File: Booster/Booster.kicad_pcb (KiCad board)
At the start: 2 copper layers, 100 x 100 mm, 113 parts, among them IC401 SN754410, J101 Track, J301 15VDC, J601 StatusLED, J701 Conn_01x04, P201 CONN_01X02, P202 CONN_01X02, P601 ~OVERCURRENT_OUT, P602 ~OVERCURRENT_OUT_OP, P603 MSTR_SW, P604 MSTR_SW_OUT, P605 MSTR_SW_OUT_OP, P606 ~DRIVER_ENABLE_OUT_OP, P607 ~DRIVER_ENABLE_OUT, P701 REVERSER_OUT, P702 REVERSER_OUT_OP, Q601 BC807-40, Q602 BC807-40, Q603 BC807-40, Q604 BC817-40, Q701 BC817-40, SW601 DIP, U201 6N137, U203 LM339, U301 LM7805_TO220, U501 LM338, U502 LM358, U503 NE555, U504 74HC08, U602 PC817, U603 PC817, U604 PC817, U701 74HC86, U702 PC817

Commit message: Still working on PCB layout
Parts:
- added REF**: 1pin, Connectors:1pin, F.Cu at (130.0, 145.0)
- added REF**: 1pin, Connectors:1pin, F.Cu at (45.0, 145.0)
- moved R708 222.6 mm to (44.0, 117.0)
- moved D701 207.8 mm to (44.0, 108.0)
- moved P202 188.3 mm to (109.0, 85.5), turned to 90 degrees
- moved R614 170.6 mm to (41.0, 90.0)
- moved D601 165.3 mm to (47.5, 98.0), turned to 180 degrees
- moved R603 160.5 mm to (48.0, 113.0)
- moved R607 158.3 mm to (49.0, 90.0)
- moved U702 156.1 mm to (97.0, 92.6), turned to 90 degrees
- moved R608 155.0 mm to (48.0, 79.0)
- moved Q701 150.3 mm to (94.0, 89.0)
- moved P701 149.7 mm to (95.0, 76.5), turned to 90 degrees
- moved U602 147.1 mm to (55.5, 100.6), turned to 90 degrees
- moved R705 145.0 mm to (123.0, 83.0)
- moved R601 143.2 mm to (54.0, 110.0)
- moved J601 143.1 mm to (49.0, 85.0), turned to 180 degrees
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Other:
- outline, holes or cut-outs redrawn

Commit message: Starting to add traces. Minor schematic changes to aid routing.
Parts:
- added REF**: Heatshield, Trainiot:Single_Pin_Heatshield, F.Cu at (50.5, 119.5)
- added TP511: TEST, Measurement_Points:Measurement_Point_Round-TH_Small, B.Cu at (123.5, 138.0)
- C301, C302, C502, C506, D301, IC401, J101, J301, RV501, RV502, RV503, RV504, RV701, TP501, TP503, TP504, TP505, TP507, U501: moved to B.Cu
- R508, R509: footprint Resistors_SMD:R_0805 -> Resistors_THT:R_Axial_DIN0207_L6.3mm_D2.5mm_P7.62mm_Horizontal
- U201: footprint Housings_DIP:DIP-8_W7.62mm -> Housings_DIP:SMDIP-8_W9.53mm_Clearance8mm
- U301: footprint TO_SOT_Packages_THT:TO-220-3_Vertical -> TO_SOT_Packages_SMD:SOT-89-3
- U602, U603, U604, U702: footprint Housings_DIP:DIP-4_W7.62mm -> Housings_DIP:SMDIP-4_W9.53mm_Clearance8mm
- moved D201 220.7 mm to (82.8, 121.5)
- moved R204 215.6 mm to (93.5, 140.4), turned to 90 degrees
- moved D202 214.6 mm to (94.5, 97.0)
- moved R205 211.0 mm to (90.0, 135.4), turned to 90 degrees
- moved C202 206.9 mm to (101.0, 107.0)
- moved C201 200.2 mm to (114.0, 97.5)
- moved C401 189.2 mm to (43.5, 140.0)
- moved R704 181.9 mm to (83.0, 107.5)
- moved C402 172.2 mm to (65.0, 131.5)
- moved R707 163.1 mm to (94.5, 83.5)
- moved R702 154.1 mm to (114.0, 87.5)
- moved R609 110.4 mm to (82.0, 94.5)
- moved R610 82.0 mm to (119.0, 83.0)
- moved C601 58.1 mm to (167.8, 63.3)
- moved R201 58.1 mm to (264.5, 80.3)
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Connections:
- R502 pad 1: Net-(R502-Pad1) -> GND
- R502 pad 2: Net-(R501-Pad1) -> Net-(R502-Pad2)
- REF** pad 1: (no net) -> GND (x2)
- RV501 pad 1: GND -> Net-(R502-Pad2)
- RV501 pad 2: GND -> Net-(R502-Pad2)
- RV501 pad 3: Net-(R502-Pad1) -> Net-(R501-Pad1)
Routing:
- net +5V: track 0.00 -> 96.7 mm
- net +15V: track 0.00 -> 57.3 mm
- net /Driver/VCC_DRIVER: track 0.00 -> 41.0 mm
- net Net-(R503-Pad2): track 0.00 -> 38.5 mm, vias 0 -> 2
- net Net-(R505-Pad1): track 0.00 -> 31.7 mm
- net Net-(C507-Pad1): track 0.00 -> 30.4 mm
- net /Driver/DRIVER_ENABLE: track 0.00 -> 28.9 mm
- net GND: track 0.00 -> 23.4 mm
- net Net-(R503-Pad1): track 0.00 -> 20.4 mm
- net /Driver/TrackB: track 0.00 -> 16.9 mm
- net /Driver/TrackA: track 0.00 -> 15.8 mm
- net Net-(C502-Pad1): track 0.00 -> 14.4 mm
- net /Driver/DRIVER_SIGNAL: track 0.00 -> 14.2 mm
- net /DCC Input/REF_1.35V: track 0.00 -> 7.71 mm
- net Net-(R505-Pad2): track 0.00 -> 7.66 mm
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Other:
- net class HighAmp added: clearance 0.5, trace_width 3.5, via_dia 0.8, via_drill 0.6
- board text added: "15VDC"
- board text added: "A-Track-B"
- board text added: "GND"

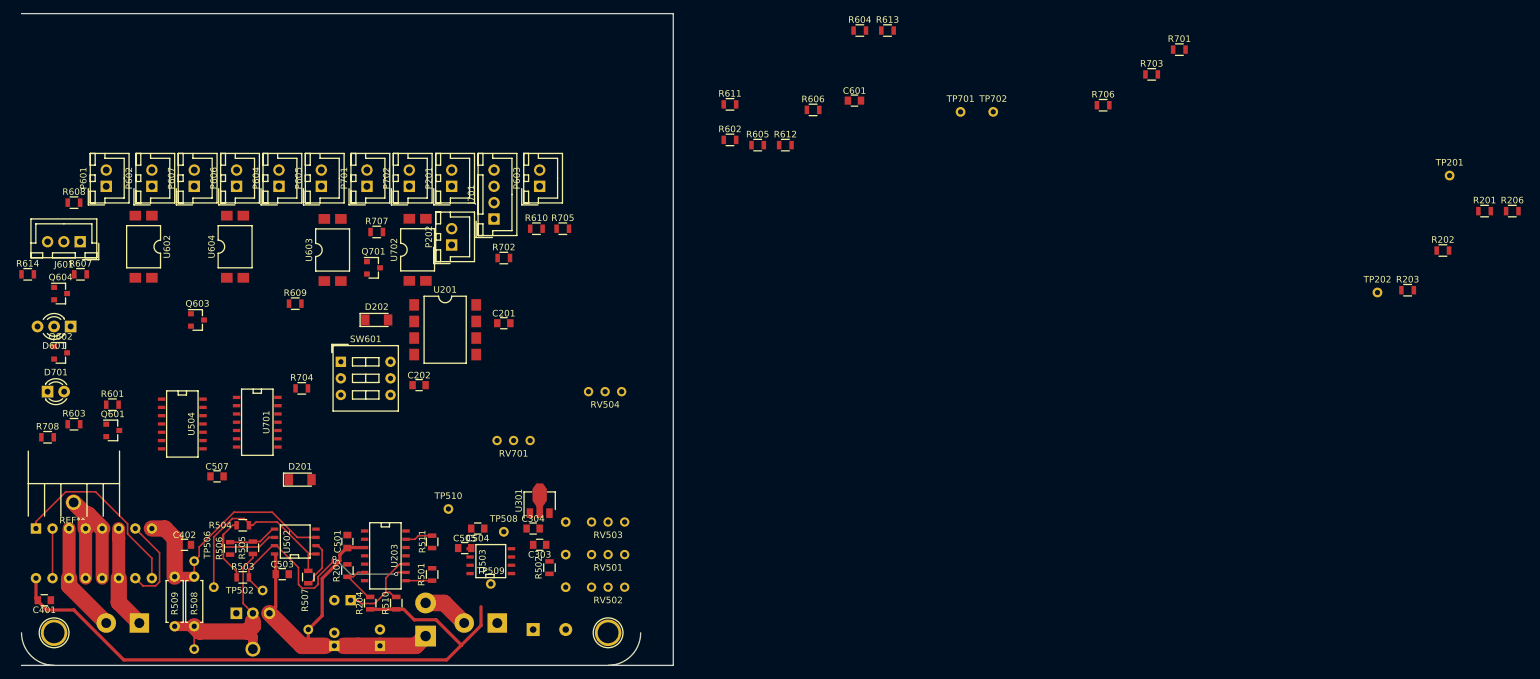
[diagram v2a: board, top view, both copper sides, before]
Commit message: First full layout pass of the PCB.
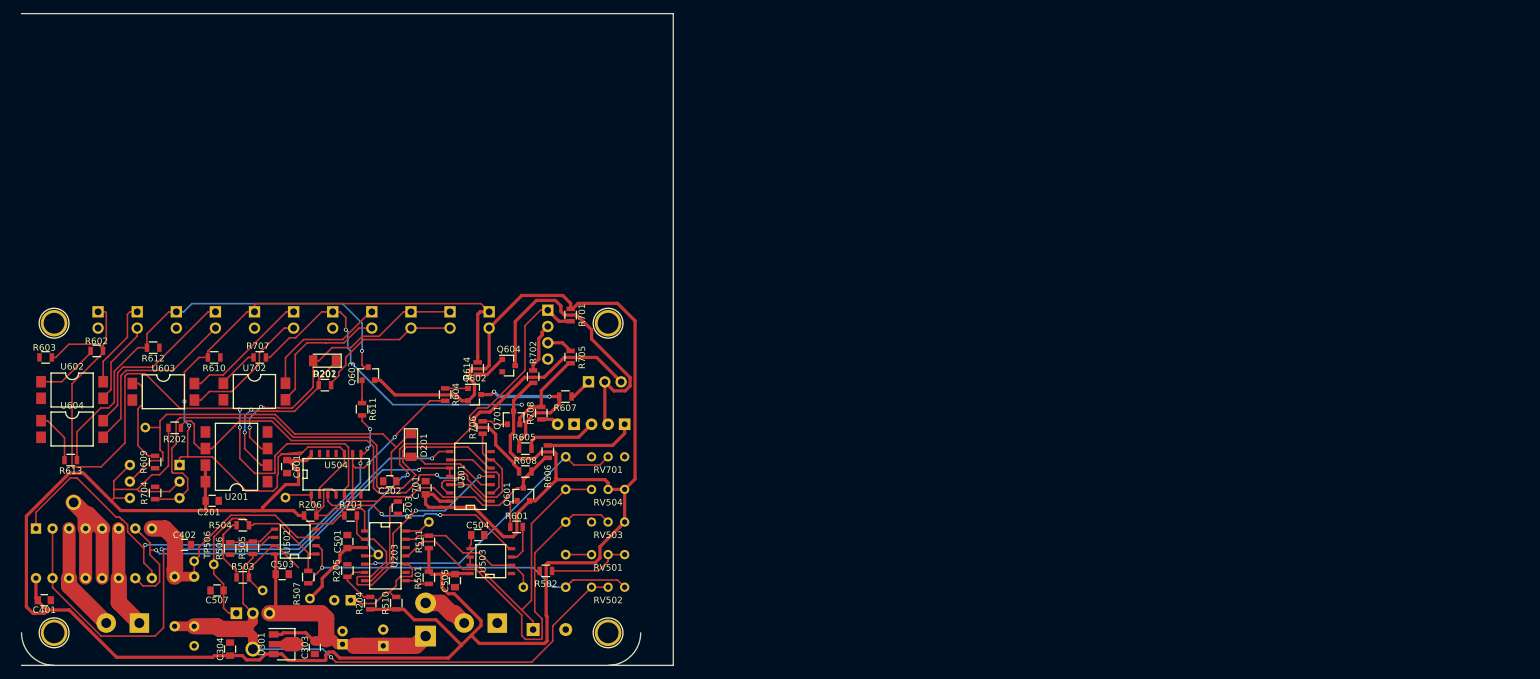
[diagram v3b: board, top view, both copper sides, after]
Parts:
- added C701: 100nF, Capacitors_SMD:C_0805, F.Cu at (102.0, 122.8)
- added REF**: 1pin, Connectors:1pin, F.Cu at (45.0, 97.5)
- added REF**: 1pin, Connectors:1pin, F.Cu at (130.0, 97.5)
- D601, D701, J601, J701, P201, P202, P601, P602, P603, P604, P605, P606, P607, P701, P702, R508, R509, REF**, SW601, TP201, TP202, TP502, TP508, TP509, TP510, TP701, TP702: moved to B.Cu
- moved TP201 203.8 mm to (59.0, 113.5)
- moved R202 196.5 mm to (63.5, 113.5)
- moved R206 190.3 mm to (84.3, 127.0)
- moved R201 179.9 mm to (86.5, 107.0)
- moved TP202 170.5 mm to (80.5, 124.2)
- moved R203 158.5 mm to (97.8, 125.8), turned to 270 degrees
- moved R613 141.6 mm to (47.5, 118.5), turned to 180 degrees
- moved R703 140.3 mm to (90.5, 127.0)
- moved TP702 116.2 mm to (94.8, 133.0)
- moved R706 107.3 mm to (110.8, 113.5), turned to 270 degrees
- moved C601 103.6 mm to (80.8, 119.5), turned to 270 degrees
- moved R602 102.4 mm to (51.5, 101.8)
- moved R701 101.9 mm to (124.2, 96.2), turned to 90 degrees
- moved R612 101.9 mm to (60.2, 101.2), turned to 180 degrees
- moved D601 86.3 mm to (132.5, 113.0)
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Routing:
- net +5V: track 96.7 -> 457.1 mm
- net /Status/STATUS_GREEN_LED: track 0.00 -> 150.1 mm, vias 0 -> 2
- net /Overcurrent Detector/MSTR_SW: track 0.00 -> 120.9 mm, vias 0 -> 2
- net Net-(IC401-Pad15): track 7.62 -> 92.3 mm, vias 0 -> 2
- net Net-(R704-Pad1): track 0.00 -> 83.9 mm
- net Net-(C202-Pad1): track 0.00 -> 77.6 mm
- net Net-(P607-Pad1): track 0.00 -> 69.0 mm, vias 0 -> 1
- net /DCC Input/DCC: track 0.00 -> 68.1 mm, vias 0 -> 2
- net Net-(P701-Pad1): track 0.00 -> 65.3 mm, vias 0 -> 2
- net /Reversing/PhotoDiode: track 0.00 -> 63.2 mm, vias 0 -> 1
- net Net-(RV503-Pad2): track 0.00 -> 57.6 mm
- net Net-(R505-Pad1): track 31.7 -> 89.3 mm, vias 0 -> 1
- net /Driver/DRIVER_SIGNAL: track 14.2 -> 67.2 mm, vias 0 -> 2
- net /Driver/DRIVER_ENABLE: track 28.9 -> 80.9 mm, vias 0 -> 4
- net Net-(R507-Pad1): track 7.40 -> 56.0 mm, vias 0 -> 1
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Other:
- rule trace_min: 0.254 -> 0.25

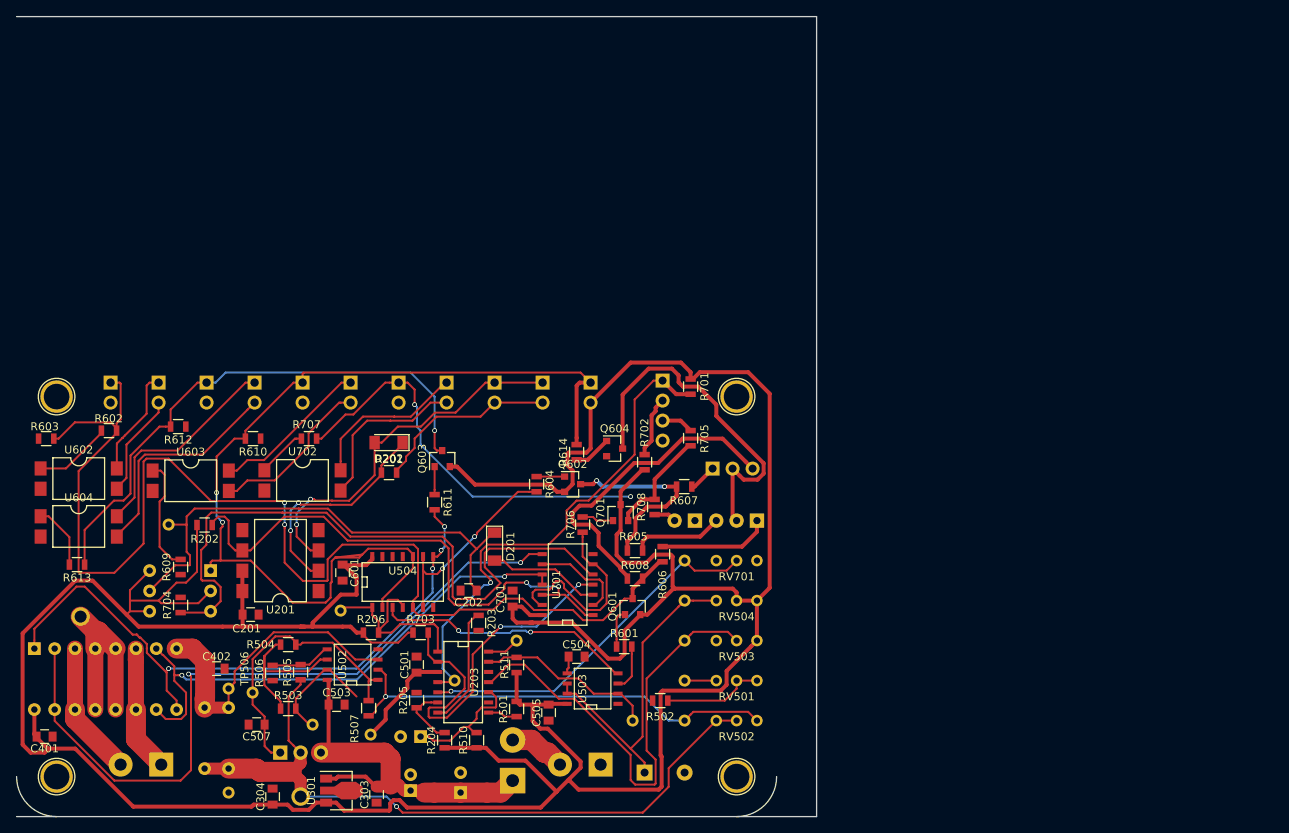
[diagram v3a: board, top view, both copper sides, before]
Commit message: Made board slightly larger to have more space along the edge. It is now 9.7 x 6 cm
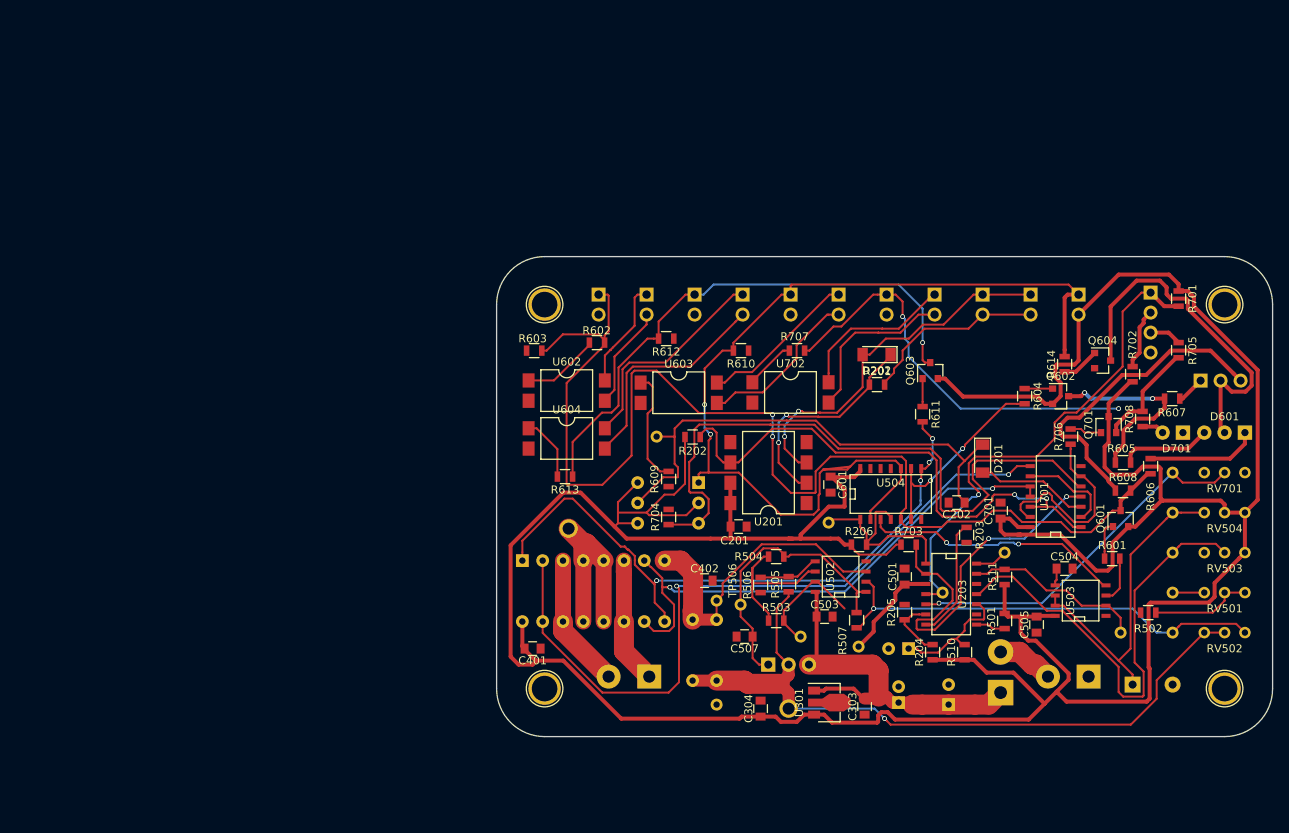
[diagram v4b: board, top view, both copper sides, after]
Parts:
- moved REF** 62.1 mm to (106.0, 86.0)
- moved REF** 62.1 mm to (191.0, 86.0)
- moved C201 62.0 mm to (130.2, 113.8)
- moved C202 62.0 mm to (157.5, 110.8)
- moved C301 62.0 mm to (156.5, 136.0)
- moved C302 62.0 mm to (150.2, 135.8)
- moved C303 62.0 mm to (146.0, 136.2)
- moved C304 62.0 mm to (133.0, 136.5)
- moved C401 62.0 mm to (104.5, 129.0)
- moved C402 62.0 mm to (126.0, 120.5)
- moved C501 62.0 mm to (151.0, 120.0)
- moved C502 62.0 mm to (151.5, 129.0)
- moved C503 62.0 mm to (141.0, 125.0)
- moved C504 62.0 mm to (171.0, 119.0)
- moved C505 62.0 mm to (167.5, 126.0)
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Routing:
- net +5V: track 457.1 -> 452.3 mm
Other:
- board size 100 x 100 mm -> 97 x 60 mm

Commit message: Minor adjustments to traces
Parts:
- moved TP509 13.8 mm to (167.5, 118.0)
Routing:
- net Net-(P602-Pad2): track 12.9 -> 0.14 mm
- net Net-(P701-Pad1): track 65.3 -> 66.9 mm
- net Net-(P702-Pad1): track 20.1 -> 19.4 mm

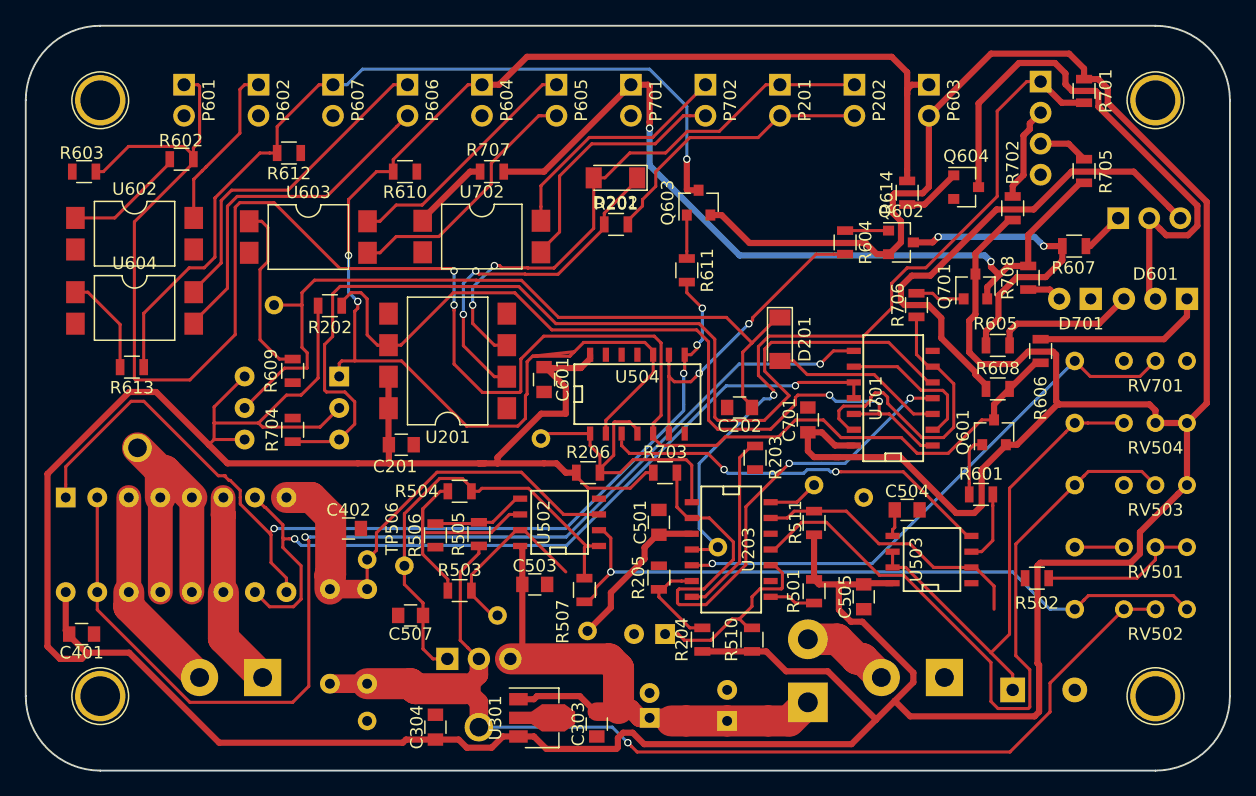
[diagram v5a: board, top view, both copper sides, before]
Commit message: Added gnd plane, starting to hook up gnd pads.
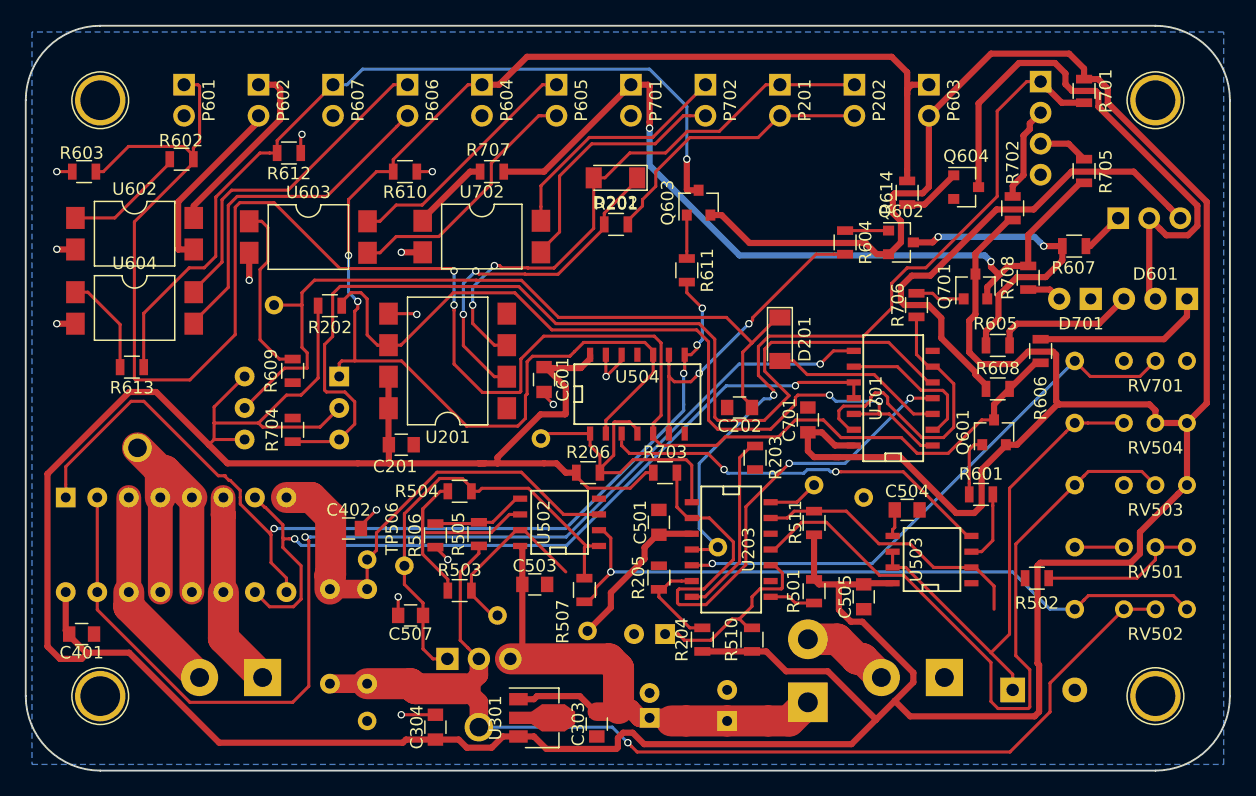
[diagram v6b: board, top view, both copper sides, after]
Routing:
- net GND: track 23.4 -> 49.7 mm, vias 0 -> 14
- net Net-(P602-Pad2): track 0.14 -> 14.7 mm
- net /Overcurrent Detector/MSTR_SW: track 121.3 -> 118.5 mm
- net Net-(P602-Pad1): track 13.6 -> 15.1 mm
- net Net-(P607-Pad1): track 69.2 -> 68.5 mm
- added copper zone on B.Cu, net GND
